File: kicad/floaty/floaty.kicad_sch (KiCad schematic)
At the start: 29 parts, among them IC1 DW01A, J1 TYPE-C-31-M-12, Q1 FS8205A, Q2 AO3401A, U1 TP4056, U2 MPU-6050, U3 HT7333, U4 E73-2G4M08S1C

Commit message: First routing
Sort of works, but can be improved.
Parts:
- added C10, C11: 0.1u, Capacitor_SMD:C_0402_1005Metric, symbol Device:C_Small
- added C12: 2.2n, Capacitor_SMD:C_0402_1005Metric, symbol Device:C_Small
- added C6, C7: 12p, Capacitor_SMD:C_0402_1005Metric, symbol Device:C_Small
- added C8: 100n, Capacitor_SMD:C_0402_1005Metric, symbol Device:C_Small
- added C9: 10n, Capacitor_SMD:C_0402_1005Metric, symbol Device:C_Small
- added R12, R13: 10k, Resistor_SMD:R_0402_1005Metric, symbol Device:R_Small_US
- added TP1, TP2, TP3, TP4, TP5: TestPoint, TestPoint:TestPoint_Pad_D1.5mm, symbol Connector:TestPoint
- added U5: SHT30-DIS, Sensor_Humidity:Sensirion_DFN-8-1EP_2.5x2.5mm_P0.5mm_EP1.1x1.7mm, symbol Sensor_Humidity:SHT30-DIS
- added Y1: 32.768 kHz, XTAL_NX3215SA-32.768K-STD-MUA-14, symbol NX3215SA-32.768K-STD-MUA-14:NX3215SA-32.768K-STD-MUA-14
- U4: footprint E73-2G4M08S1C -> lib:E73-2G4M08S1C-modified
- gave numbers to parts that had none: 2
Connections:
- net +3V0: now also U2.13 (VDD), U2.8 (VDDIO), C10.1, C8.2, C9.2, R12.2, R13.1, TP5.1, U5.5 (VDD)
- net GND: now also U1.1 (TEMP), U2.1 (CLKIN), U2.11 (FSYNC), U2.18 (GND), U2.9 (AD0), C10.2, C11.2, C12.1, C6.1, C7.1, C8.1, C9.1, TP2.1, U5.2 (ADDR), U5.7 (R), U5.8 (VSS), U5.9 (VSS)
- net SDA: now reaches U4.17 (P1.09)
- net SDA: now also U2.24 (SDA), R12.1, U5.1 (SDA)
- net at U2.10 (REGOUT): now also C11.1
- net IMU_INT: now reaches U2.12 (INT)
- net IMU_INT: now also U4.8 (P0.29/AIN5)
- net at U2.20 (CPOUT): now also C12.2
- net SCL: now reaches U2.23 (SCL)
- net SCL: now also U4.15 (P0.05/AIN3), R13.2, U5.4 (SCL)
- net at U4.11 (P0.00/XL1): now also C6.2, Y1.2
- net at U4.13 (P0.01/XL2): now also C7.2, Y1.1
- net RESET: now reaches U4.26 (P0.18/RESET)
- net RESET: now also TP1.1
- net SWDIO: now reaches U4.37 (SWDIO)
- net SWDIO: now also TP4.1
- net SWDCLK: now reaches U4.39 (SWDCLK)
- net SWDCLK: now also TP3.1
- no-connect marks 5 -> 34
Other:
- note added: "I2C pullups"
- note added: "IMU - Accelerometer + Gyroscope"
- note added: "SWD programming test points"
- note added: "Status LED"
- note added: "Temperature sensor"
- note added: "nRF52840 SoC"
- moved on the sheet: D4, J1, R10, R11, R9, U2, U4A, U4B, U4C

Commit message: Better routing
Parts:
- U3: value HT7333 -> HT7330; LCSC C21583 -> C347190
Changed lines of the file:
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@@
       (effects (font (size 1.27 1.27)) hide)
     )
-    (property "Datasheet" "https://store.invensense.com/datasheets/invensense/MPU-6050_DataSheet_V3%204.pdf" (id 3) (at 336.55 194.31 0)
+    (property "Datasheet" "https://invensense.tdk.com/wp-content/uploads/2015/02/MPU-6000-Datasheet1.pdf" (id 3) (at 336.55 194.31 0)
       (effects (font (size 1.27 1.27)) hide)
     )
@@
       (effects (font (size 1.27 1.27)) (justify left bottom))
     )
-    (property "Value" "HT7333" (id 1) (at 156.21 185.42 0)
+    (property "Value" "HT7330" (id 1) (at 156.21 185.42 0)
       (effects (font (size 1.27 1.27)) (justify left bottom))
     )
@@
       (effects (font (size 1.27 1.27)) (justify left bottom) hide)
     )
-    (property "LCSC" "C21583" (id 4) (at 152.4 191.77 0)
+    (property "LCSC" "C347190" (id 4) (at 152.4 191.77 0)
       (effects (font (size 1.27 1.27)) hide)
     )
@@
     )
     (path "/c7c193a2-5212-4417-8506-9312668d4eea"
-      (reference "U3") (unit 1) (value "HT7333") (footprint "lib:SOT89")
+      (reference "U3") (unit 1) (value "HT7330") (footprint "lib:SOT89")
     )
     (path "/d2fbb124-5e02-43b3-9d0a-6928bc24c6c7"

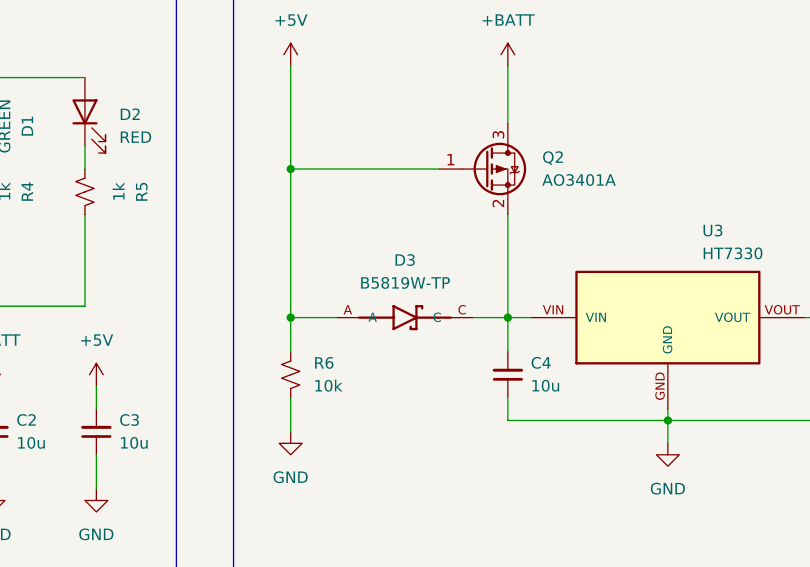
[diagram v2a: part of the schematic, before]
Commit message: Added LCSC part numbers to all components
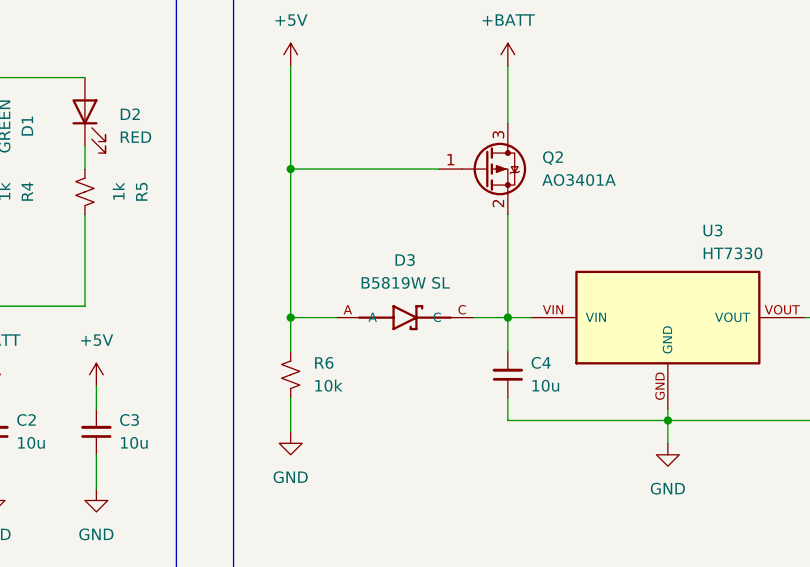
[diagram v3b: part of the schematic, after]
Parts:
- C1, C10, C11, C8: LCSC (none) -> C1525
- C12: LCSC (none) -> C1531
- C2, C3, C4, C5: LCSC (none) -> C15525
- C9: LCSC (none) -> C15195
- D3: value B5819W-TP -> B5819W SL; LCSC (none) -> C8598
- J1: LCSC (none) -> C165948
- R1: LCSC (none) -> C25076
- R10, R9: LCSC (none) -> C25905
- R11, R2, R4, R5: LCSC (none) -> C11702
- R12, R13, R6: LCSC (none) -> C25744
- R3: LCSC (none) -> C4109
- R7, R8: LCSC (none) -> C25790
- U4: LCSC (none) -> C356849
- U5: LCSC (none) -> C2687423
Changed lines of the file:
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@@
+      (effects (font (size 1.27 1.27)) hide)
+    )
+    (property "LCSC" "C1525" (id 4) (at 287.02 205.74 0)
       (effects (font (size 1.27 1.27)) hide)
     )
@@
       (effects (font (size 1.27 1.27)) hide)
     )
+    (property "LCSC" "C11702" (id 4) (at 87.63 177.8 90)
+      (effects (font (size 1.27 1.27)) hide)
+    )
     (pin "1")
     (pin "2")
@@
     )
     (property "Datasheet" "https://www.sensirion.com/fileadmin/user_upload/customers/sensirion/Dokumente/2_Humidity_Sensors/Datasheets/Sensirion_Humidity_Sensors_SHT3x_Datasheet_digital.pdf" (id 3) (at 274.32 180.34 0)
+      (effects (font (size 1.27 1.27)) hide)
+    )
+    (property "LCSC" "C2687423" (id 4) (at 274.32 181.61 0)
       (effects (font (size 1.27 1.27)) hide)
     )
@@
       (effects (font (size 1.27 1.27)) hide)
     )
+    (property "LCSC" "C4109" (id 4) (at 26.67 198.12 0)
+      (effects (font (size 1.27 1.27)) hide)
+    )
     (pin "1")
     (pin "2")
@@
       (effects (font (size 1.27 1.27)) hide)
     )
+    (property "LCSC" "C11702" (id 4) (at 74.93 177.8 90)
+      (effects (font (size 1.27 1.27)) hide)
+    )
     (pin "1")
     (pin "2")
@@
     )
     (property "Datasheet" "~" (id 3) (at 118.11 257.81 0)
+      (effects (font (size 1.27 1.27)) hide)
+    )
+    (property "LCSC" "C25790" (id 4) (at 118.11 257.81 0)
       (effects (font (size 1.27 1.27)) hide)
     )
@@
     (in_bom yes) (on_board yes) (fields_autoplaced)
     (property "Reference" "D3" (id 0) (at 123.19 185.42 0))
-    (property "Value" "B5819W-TP" (id 1) (at 123.19 187.96 0))
+    (property "Value" " B5819W SL" (id 1) (at 123.19 187.96 0))
     (property "Footprint" "SOD3716X135N" (id 2) (at 123.19 191.77 0)
       (effects (font (size 1.27 1.27)) (justify left bottom) hide)
@@
     (property "MANUFACTURER" "Micro Commercial Components" (id 4) (at 123.19 191.77 0)
       (effects (font (size 1.27 1.27)) (justify left bottom) hide)
+    )
+    (property "LCSC" "C8598" (id 5) (at 123.19 191.77 0)
+      (effects (font (size 1.27 1.27)) hide)
     )
     (pin "A")
@@
       (effects (font (size 1.27 1.27)) hide)
     )
+    (property "LCSC" "C11702" (id 4) (at 85.09 240.03 90)
+      (effects (font (size 1.27 1.27)) hide)
+    )
     (pin "1")
     (pin "2")
@@
     )
     (property "Datasheet" "~" (id 3) (at 200.66 189.23 0)
+      (effects (font (size 1.27 1.27)) hide)
+    )
+    (property "LCSC" "C11702" (id 4) (at 200.66 189.23 90)
       (effects (font (size 1.27 1.27)) hide)
     )
@@
       (effects (font (size 1.27 1.27)) hide)
     )
+    (property "LCSC" "C25744" (id 4) (at 232.41 185.42 90)
+      (effects (font (size 1.27 1.27)) hide)
+    )
     (pin "1")
     (pin "2")
@@
       (effects (font (size 1.27 1.27)) hide)
     )
+    (property "LCSC" "C15195" (id 4) (at 327.66 167.64 0)
+      (effects (font (size 1.27 1.27)) hide)
+    )
     (pin "1")
     (pin "2")
@@
       (effects (font (size 1.27 1.27)) hide)
     )
+    (property "LCSC" "C25744" (id 4) (at 110.49 198.12 0)
+      (effects (font (size 1.27 1.27)) hide)
+    )
     (pin "1")
     (pin "2")
@@
     )
     (property "Datasheet" "~" (id 3) (at 171.45 196.85 0)
+      (effects (font (size 1.27 1.27)) hide)
+    )
+    (property "LCSC" "C15525" (id 4) (at 171.45 196.85 0)
       (effects (font (size 1.27 1.27)) hide)
     )
@@
       (effects (font (size 1.27 1.27)) hide)
     )
+    (property "LCSC" "C25905" (id 4) (at 208.28 54.61 90)
+      (effects (font (size 1.27 1.27)) hide)
+    )
     (pin "1")
     (pin "2")
@@
       (effects (font (size 1.27 1.27)) hide)
     )
+    (property "LCSC" "C1525" (id 4) (at 40.64 247.65 0)
+      (effects (font (size 1.27 1.27)) hide)
+    )
     (pin "1")
     (pin "2")
@@
     )
     (property "Datasheet" "~" (id 3) (at 36.83 240.03 0)
+      (effects (font (size 1.27 1.27)) hide)
+    )
+    (property "LCSC" "C25076" (id 4) (at 36.83 240.03 90)
       (effects (font (size 1.27 1.27)) hide)
     )
@@
       (effects (font (size 1.27 1.27)) hide)
     )
+    (property "LCSC" "C1525" (id 4) (at 344.17 167.64 0)
+      (effects (font (size 1.27 1.27)) hide)
+    )
     (pin "1")
     (pin "2")
@@
       (effects (font (size 1.27 1.27)) hide)
     )
+    (property "LCSC" "C25790" (id 4) (at 118.11 247.65 0)
+      (effects (font (size 1.27 1.27)) hide)
+    )
     (pin "1")
     (pin "2")
@@
     )
     (property "Datasheet" "~" (id 3) (at 134.62 198.12 0)
+      (effects (font (size 1.27 1.27)) hide)
+    )
+    (property "LCSC" "C15525" (id 4) (at 134.62 198.12 0)
       (effects (font (size 1.27 1.27)) hide)
     )
@@
     (property "MAXIMUM_PACKAGE_HEIGHT" "3.31mm" (id 7) (at 181.61 46.99 0)
       (effects (font (size 1.27 1.27)) (justify left bottom) hide)
+    )
+    (property "LCSC" "C165948" (id 8) (at 181.61 46.99 0)
+      (effects (font (size 1.27 1.27)) hide)
     )
     (pin "A1B12")
@@
       (effects (font (size 1.27 1.27)) hide)
     )
+    (property "LCSC" "C25744" (id 4) (at 234.95 185.42 90)
+      (effects (font (size 1.27 1.27)) hide)
+    )
     (pin "1")
     (pin "2")
@@
       (effects (font (size 1.27 1.27)) hide)
     )
+    (property "LCSC" "C25905" (id 4) (at 153.67 27.94 90)
+      (effects (font (size 1.27 1.27)) hide)
+    )
     (pin "1")
     (pin "2")
@@
     )
     (property "Datasheet" "~" (id 3) (at 355.6 204.47 0)
+      (effects (font (size 1.27 1.27)) hide)
+    )
+    (property "LCSC" "C1525" (id 4) (at 355.6 204.47 0)
       (effects (font (size 1.27 1.27)) hide)
     )
@@
     )
     (property "Datasheet" "~" (id 3) (at 77.47 204.47 0)
+      (effects (font (size 1.27 1.27)) hide)
+    )
+    (property "LCSC" "C15525" (id 4) (at 77.47 204.47 0)
       (effects (font (size 1.27 1.27)) hide)
     )
@@
       (effects (font (size 1.27 1.27)) (justify left bottom) hide)
     )
+    (property "LCSC" "C356849" (id 4) (at 62.23 76.2 0)
+      (effects (font (size 1.27 1.27)) hide)
+    )
     (pin "19")
     (pin "21")
@@
       (effects (font (size 1.27 1.27)) hide)
     )
+    (property "LCSC" "C1531" (id 4) (at 361.95 204.47 0)
+      (effects (font (size 1.27 1.27)) hide)
+    )
     (pin "1")
     (pin "2")
@@
     )
     (property "Datasheet" "~" (id 3) (at 88.9 204.47 0)
+      (effects (font (size 1.27 1.27)) hide)
+    )
+    (property "LCSC" "C15525" (id 4) (at 88.9 204.47 0)
       (effects (font (size 1.27 1.27)) hide)
     )
@@
     )
     (path "/2030a47c-0992-40aa-885c-5a9dfccd89b0"
-      (reference "D3") (unit 1) (value "B5819W-TP") (footprint "SOD3716X135N")
+      (reference "D3") (unit 1) (value " B5819W SL") (footprint "SOD3716X135N")
     )
     (path "/d089623a-2a8c-4cf8-ad26-ece05e71838a"
